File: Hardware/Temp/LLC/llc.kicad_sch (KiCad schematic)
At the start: 23 parts, among them M1 650 V, 24 A, M2 650 V, 24 A, U1 IR2101, U2 OPAMP_OP07CSZ

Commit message: 1
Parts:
- removed C1: 2.2uF, Capacitor_SMD:C_0805_2012Metric_Pad1.18x1.45mm_HandSolder, symbol charge_battery_sym_lib:Ceramic_Cap_Hole_1uF_50V_
- removed D1: MUR1100E, Diode_THT:D_DO-41_SOD81_P10.16mm_Horizontal, symbol Diode:UF5401
- removed R1, R2: 100R_1_4W_1%, charge_battery_footprint_lib:Res_220R_1_4W_1%, symbol charge_battery_sym_lib:Res_hole_220R_1/4W_1%
- removed R3, R4: 10K_1/4W_1%, charge_battery_footprint_lib:Res_10K_1_4W_1%, symbol charge_battery_sym_lib:Res_hole_10K_1/4W_1%
- removed R5, R6, R8: 100K/1%/1_10W, charge_battery_footprint_lib:Res_200K_0603, symbol charge_battery_sym_lib:Res_200K_0603_1%
- removed R7: 10K/1%/1_10W, charge_battery_footprint_lib:Res_10K_0603, symbol charge_battery_sym_lib:Res_10K_0603_1%
- removed U1: IR2101, charge_battery_footprint_lib:IR2101, symbol charge_battery_sym_lib:IR2101
- removed U2: OPAMP_OP07CSZ, charge_battery_footprint_lib:OPAMP_OP07CSZ, symbol charge_battery_sym_lib:OPAMP_OP07CSZ
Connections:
- net H_Gate_Driver: now also M1.1 (G)
- net L_Gate_Driver: now also M2.1 (G)
- net 48V renamed 24V
- net GND1 renamed PFC_GND
- net GND2 renamed GND
- net LOAD_M1_M2: no longer names the net of C7.1, M1.3 (S), M2.2 (D)
- no-connect marks 2 -> 0
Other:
- note removed: "CHỉnh zener 5V Diode chỉnh lưu"
- note removed: "FEEDBACK VOLTAGE"
- note removed: "MẠCH LLC"
- note removed: "MẠCH LÁI MOSFET"
- moved on the sheet: C3, C4, C5, C6, C7, D2, D3, L2, L3, M1, M2

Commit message: update: LLC
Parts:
- added C1: 1uF, charge_battery_footprint_lib:Ceramic_Cap_Hole_1uF_50V, symbol charge_battery_sym_lib:Ceramic_Cap_Hole_1uF_50V_
- added D1: UF5401, Diode_THT:D_DO-201AD_P15.24mm_Horizontal, symbol Diode:UF5401
- added R1, R2: 100R_1_4W_1%, charge_battery_footprint_lib:Res_220R_1_4W_1%, symbol charge_battery_sym_lib:Res_hole_220R_1/4W_1%
- added U1: IR2101, charge_battery_footprint_lib:IR2101, symbol charge_battery_sym_lib:IR2101
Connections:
- net H_Gate_Driver: now also U1.2 (HIN); no longer M1.1 (G)
- net L_Gate_Driver: now also U1.3 (LIN); no longer M2.1 (G)
- net LOAD_M1_M2: now reaches C7.1, M1.3 (S), M2.2 (D)
- net LOAD_M1_M2: now also C1.1, U1.6 (VS)
- net GND renamed GND2
- net PFC_GND renamed GND1
- net GND1: now also U1.4 (COM)
- new net: C1.2, D1.1 (K), U1.8 (VB)
- new net: M1.1 (G), R1.2
- new net: M2.1 (G), R2.2
- new net 12V_Flyback: D1.2 (A), U1.1 (VCC)
- new net OUT_M1: R1.1, U1.7 (HO)
- new net OUT_M2: R2.1, U1.5 (LO)
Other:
- moved on the sheet: C3, C4, C5, C6, C7, D2, D3, L2, L3, M1, M2

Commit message: update: LLC
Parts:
- D1: value UF5401 -> MUR1100E; footprint Diode_THT:D_DO-201AD_P15.24mm_Horizontal -> Diode_THT:D_DO-41_SOD81_P10.16mm_Horizontal
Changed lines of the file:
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@@
 		(on_board yes)
 		(dnp no)
-		(fields_autoplaced yes)
 		(property "Reference" "D2"
-			(at 146.8882 114.3 0)
+			(at 146.558 111.76 0)
 			(effects
 				(font
@@
 		)
 		(property "Value" "16 A,  1.25 V"
-			(at 146.8882 116.84 0)
+			(at 146.558 114.3 0)
 			(effects
 				(font
@@
 		)
 		(property "Supply part number" "726-IDH06G65C6XKSA1"
-			(at 139.954 108.204 0)
-			(effects
-				(font
-					(size 1.27 1.27)
-				)
-				(hide yes)
+			(at 148.0058 116.586 0)
+			(effects
+				(font
+					(size 1.27 1.27)
+				)
 			)
 		)
@@
 		)
 		(instances
+			(project "LLC"
+				(path "/1533c2b1-3008-4776-aff4-45247d8a1449"
+					(reference "D2")
+					(unit 1)
+				)
+			)
 			(project ""
 				(path "/52eaef32-c16d-4834-ac94-ac67b58aa1d2/54ec4804-2ebd-4f2b-a686-f12eb8459952"
@@
 		(fields_autoplaced yes)
 		(property "Reference" "D1"
+			(at 81.28 54.61 0)
+			(effects
+				(font
+					(size 1.27 1.27)
+				)
+			)
+		)
+		(property "Value" "MUR1100E"
 			(at 81.28 57.15 0)
 			(effects
@@
 			)
 		)
-		(property "Value" "UF5401"
+		(property "Footprint" "Diode_THT:D_DO-41_SOD81_P10.16mm_Horizontal"
+			(at 81.28 59.055 0)
+			(effects
+				(font
+					(size 1.27 1.27)
+				)
+				(hide yes)
+			)
+		)
+		(property "Datasheet" "https://www.onsemi.com/pdf/datasheet/mur180e-d.pdf"
+			(at 81.28 63.5 0)
+			(effects
+				(font
+					(size 1.27 1.27)
+				)
+				(hide yes)
+			)
+		)
+		(property "Description" "1000V_1A_DO41"
 			(at 81.28 59.69 0)
 			(effects
@@
 					(size 1.27 1.27)
 				)
-			)
-		)
-		(property "Footprint" "Diode_THT:D_DO-201AD_P15.24mm_Horizontal"
-			(at 81.28 59.055 0)
-			(effects
-				(font
-					(size 1.27 1.27)
-				)
-				(hide yes)
-			)
-		)
-		(property "Datasheet" "http://www.vishay.com/docs/88756/uf5400.pdf"
-			(at 81.28 63.5 0)
-			(effects
-				(font
-					(size 1.27 1.27)
-				)
-				(hide yes)
-			)
-		)
-		(property "Description" "100V 3A Soft Recovery Ultrafast Rectifier Diode, DO-201AD"
-			(at 81.28 63.5 0)
-			(effects
-				(font
-					(size 1.27 1.27)
-				)
-				(hide yes)
 			)
 		)
@@
 		)
 		(property "Sim.Pins" "1=K 2=A"
+			(at 81.28 63.5 0)
+			(effects
+				(font
+					(size 1.27 1.27)
+				)
+				(hide yes)
+			)
+		)
+		(property "Field7" ""
 			(at 81.28 63.5 0)
 			(effects
@@
 		(on_board yes)
 		(dnp no)
-		(fields_autoplaced yes)
 		(property "Reference" "D3"
 			(at 146.8882 129.54 0)
@@
 		)
 		(property "Value" "16 A,  1.25 V"
-			(at 146.8882 132.08 0)
+			(at 146.05 133.35 0)
 			(effects
 				(font
@@
 		)
 		(property "Supply part number" "726-IDH06G65C6XKSA1"
-			(at 139.954 123.444 0)
-			(effects
-				(font
-					(size 1.27 1.27)
-				)
-				(hide yes)
+			(at 147.066 145.034 0)
+			(effects
+				(font
+					(size 1.27 1.27)
+				)
 			)
 		)
@@
 		)
 		(instances
+			(project "LLC"
+				(path "/1533c2b1-3008-4776-aff4-45247d8a1449"
+					(reference "D3")
+					(unit 1)
+				)
+			)
 			(project "CHARGE_BATTERY"
 				(path "/52eaef32-c16d-4834-ac94-ac67b58aa1d2/54ec4804-2ebd-4f2b-a686-f12eb8459952"

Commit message: update: LLC
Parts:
- C1: value 1uF -> 2.2uF; footprint charge_battery_footprint_lib:Ceramic_Cap_Hole_1uF_50V -> Capacitor_SMD:C_0805_2012Metric_Pad1.18x1.45mm_HandSolder; Supply URL https://www.thegioiic.com/tu-gom-multilayer-1uf-50v -> https://www.thegioiic.com/tu-gom-0805-2-2uf-50v; Supply part number Tụ Gốm Multilayer 1uF 50V -> Tụ Gốm 0805 2.2uF 50V
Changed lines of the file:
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@@
 			)
 		)
-		(property "Value" "1uF "
+		(property "Value" "2.2uF "
 			(at 104.648 71.1199 90)
 			(effects
@@
 			)
 		)
-		(property "Footprint" "charge_battery_footprint_lib:Ceramic_Cap_Hole_1uF_50V"
+		(property "Footprint" "Capacitor_SMD:C_0805_2012Metric_Pad1.18x1.45mm_HandSolder"
 			(at 94.488 70.104 0)
 			(effects
@@
 			)
 		)
-		(property "Description" "1uF ±10%, code 105"
+		(property "Description" "2.2uF ±10%"
 			(at 93.98 68.834 0)
 			(effects
@@
 			)
 		)
-		(property "Supply part number" "Tụ Gốm Multilayer 1uF 50V"
+		(property "Supply part number" "Tụ Gốm 0805 2.2uF 50V"
 			(at 93.98 68.58 0)
 			(effects
@@
 			)
 		)
-		(property "Supply URL" "https://www.thegioiic.com/tu-gom-multilayer-1uf-50v"
+		(property "Supply URL" "https://www.thegioiic.com/tu-gom-0805-2-2uf-50v"
 			(at 94.488 69.85 0)
 			(effects

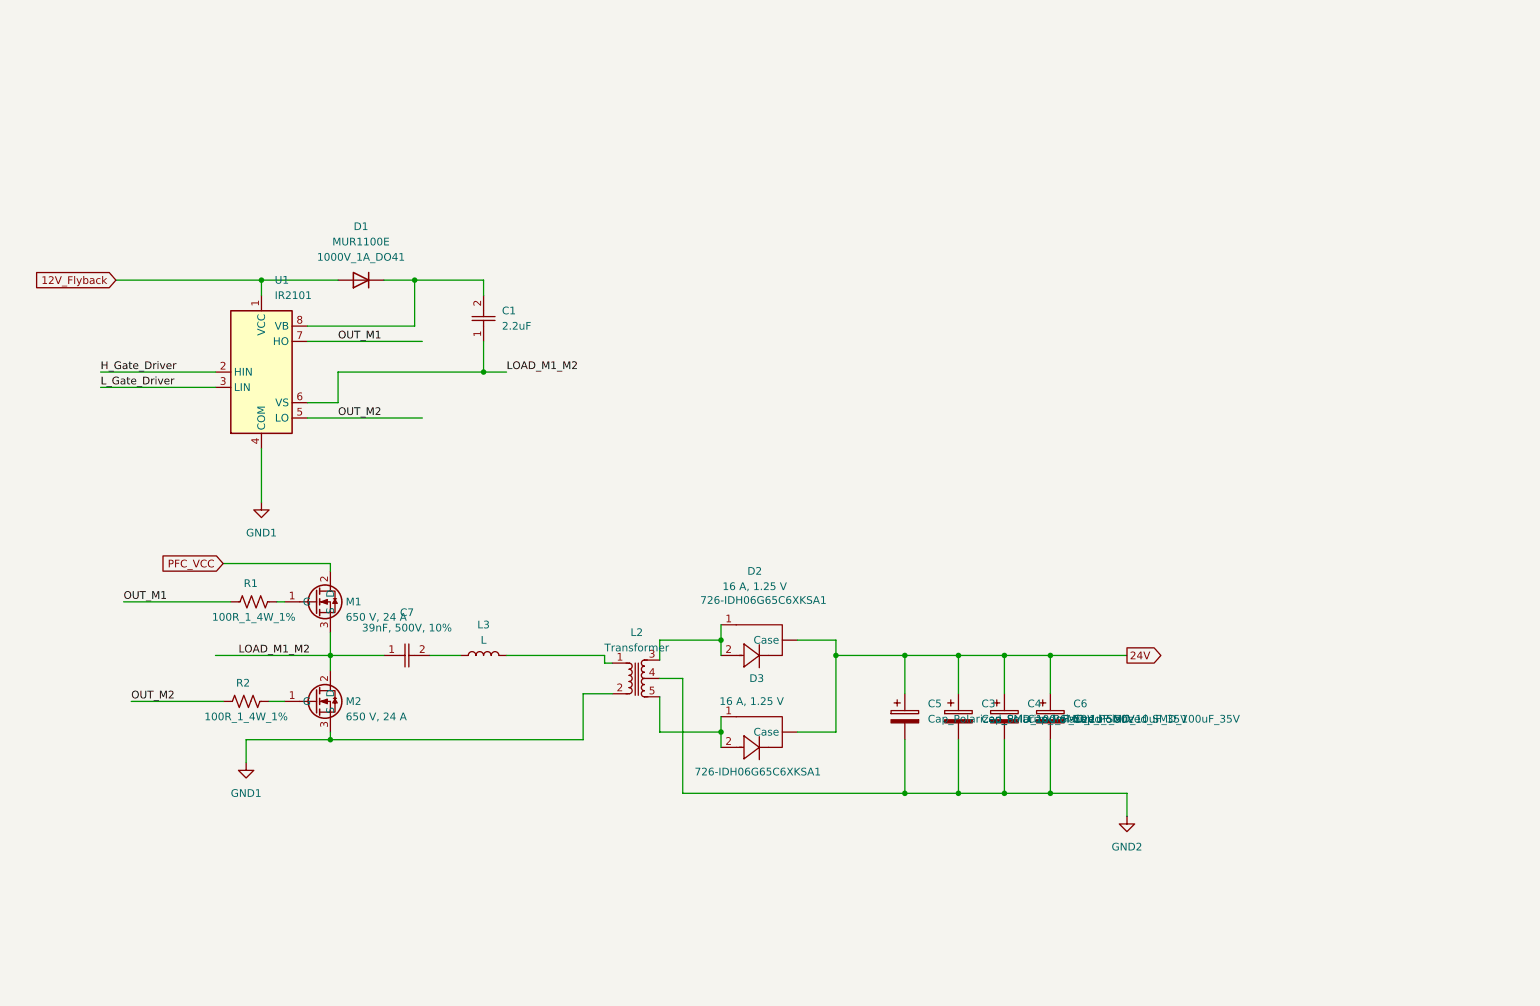
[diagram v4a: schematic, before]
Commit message: Update Schematic MCU, LLC
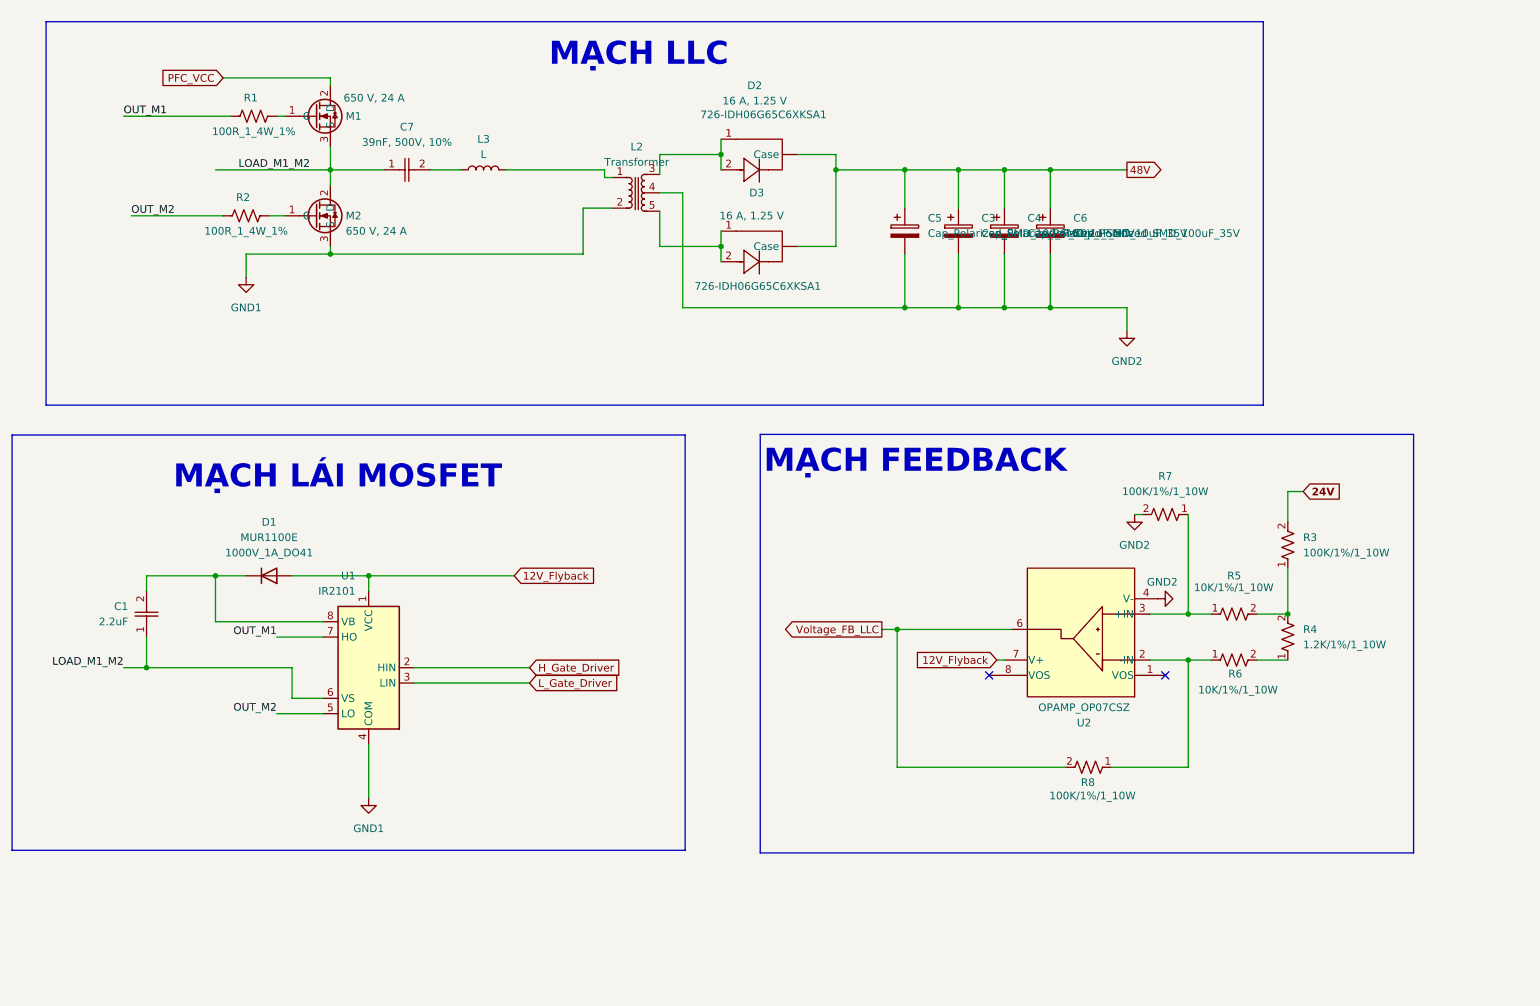
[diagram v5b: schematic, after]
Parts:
- added R3, R7, R8: 100K/1%/1_10W, charge_battery_footprint_lib:Res_200K_0603, symbol charge_battery_sym_lib:Res_200K_0603_1%
- added R4: 1.2K/1%/1_10W, charge_battery_footprint_lib:Res_200K_0603, symbol charge_battery_sym_lib:Res_200K_0603_1%
- added R5, R6: 10K/1%/1_10W, charge_battery_footprint_lib:Res_10K_0603, symbol charge_battery_sym_lib:Res_10K_0603_1%
- added U2: OPAMP_OP07CSZ, charge_battery_footprint_lib:OPAMP_OP07CSZ, symbol charge_battery_sym_lib:OPAMP_OP07CSZ
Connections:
- net 12V_Flyback: now also U2.7 (V+)
- net 24V: now also R3.2; no longer C3.1, C4.1, C5.1, C6.1, D2. (Case), D3. (Case)
- net GND2: now also R7.2, U2.4 (V-)
- new net: R4.1, R6.2
- new net: R3.1, R4.2, R5.2
- new net: R6.1, R8.1, U2.2 (-IN)
- new net: R5.1, R7.1, U2.3 (+IN)
- new net 48V: C3.1, C4.1, C5.1, C6.1, D2. (Case), D3. (Case)
- new net Voltage_FB_LLC: R8.2, U2.6
- no-connect marks 0 -> 2
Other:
- note added: "MẠCH FEEDBACK"
- note added: "MẠCH LLC"
- note added: "MẠCH LÁI MOSFET"
- moved on the sheet: C1, C3, C4, C5, C6, C7, D1, D2, D3, L2, L3, M1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

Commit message: Update LLC
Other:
- note added: "MẠCH TẠM ỔN"
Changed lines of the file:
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@@
+		)
+	)
+	(text "MẠCH TẠM ỔN"
+		(exclude_from_sim no)
+		(at 78.74 178.0286 0)
+		(effects
+			(font
+				(size 3.81 3.81)
+				(thickness 0.762)
+				(bold yes)
+			)
 		)
 	)

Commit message: hardware:sche: update schematic F4, F1
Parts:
- removed R3, R7: 100K/1%/1_10W, charge_battery_footprint_lib:Res_200K_0603, symbol charge_battery_sym_lib:Res_200K_0603_1%
- removed R4: 1.2K/1%/1_10W, charge_battery_footprint_lib:Res_200K_0603, symbol charge_battery_sym_lib:Res_200K_0603_1%
- removed R5, R6: 10K/1%/1_10W, charge_battery_footprint_lib:Res_10K_0603, symbol charge_battery_sym_lib:Res_10K_0603_1%
- added R3, R4: 10K_1/4W_1%, charge_battery_footprint_lib:Res_10K_1_4W_1%, symbol charge_battery_sym_lib:Res_hole_10K_1/4W_1%
- added R5, R6: 100K/1%/1_10W, charge_battery_footprint_lib:Res_200K_0603, symbol charge_battery_sym_lib:Res_200K_0603_1%
- added R7: 10K/1%/1_10W, charge_battery_footprint_lib:Res_10K_0603, symbol charge_battery_sym_lib:Res_10K_0603_1%
- C1: value 2.2uF -> 2.2uF
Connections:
- net 12V_Flyback: no longer U2.7 (V+)
- net 48V: now also R8.2
- net GND2: now also R4.2, R5.1, R7.1
- net at R8.1: now also R3.2, R7.2; no longer U2.2 (-IN)
- net at U2.3 (+IN): now also R3.1, R5.2
- net Voltage_FB_LLC renamed Voltage_LLC
- net Voltage_LLC: now also R6.1; no longer R8.2
- new net: R4.1, R6.2, U2.2 (-IN)
- new net 9V: U2.7 (V+)
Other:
- note added: "CHỉnh zener 5V Diode chỉnh lưu"
- note added: "FEEDBACK VOLTAGE"
- note removed: "MẠCH FEEDBACK"
- note removed: "MẠCH TẠM ỔN"
- moved on the sheet: C1, C3, C4, C5, C6, C7, D1, D2, D3, L2, L3, M1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
